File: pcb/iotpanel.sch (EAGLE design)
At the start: 33 parts, among them IC1 IC_CPLD_XC2C32A, IC4 REG1117, IC5 REG1117

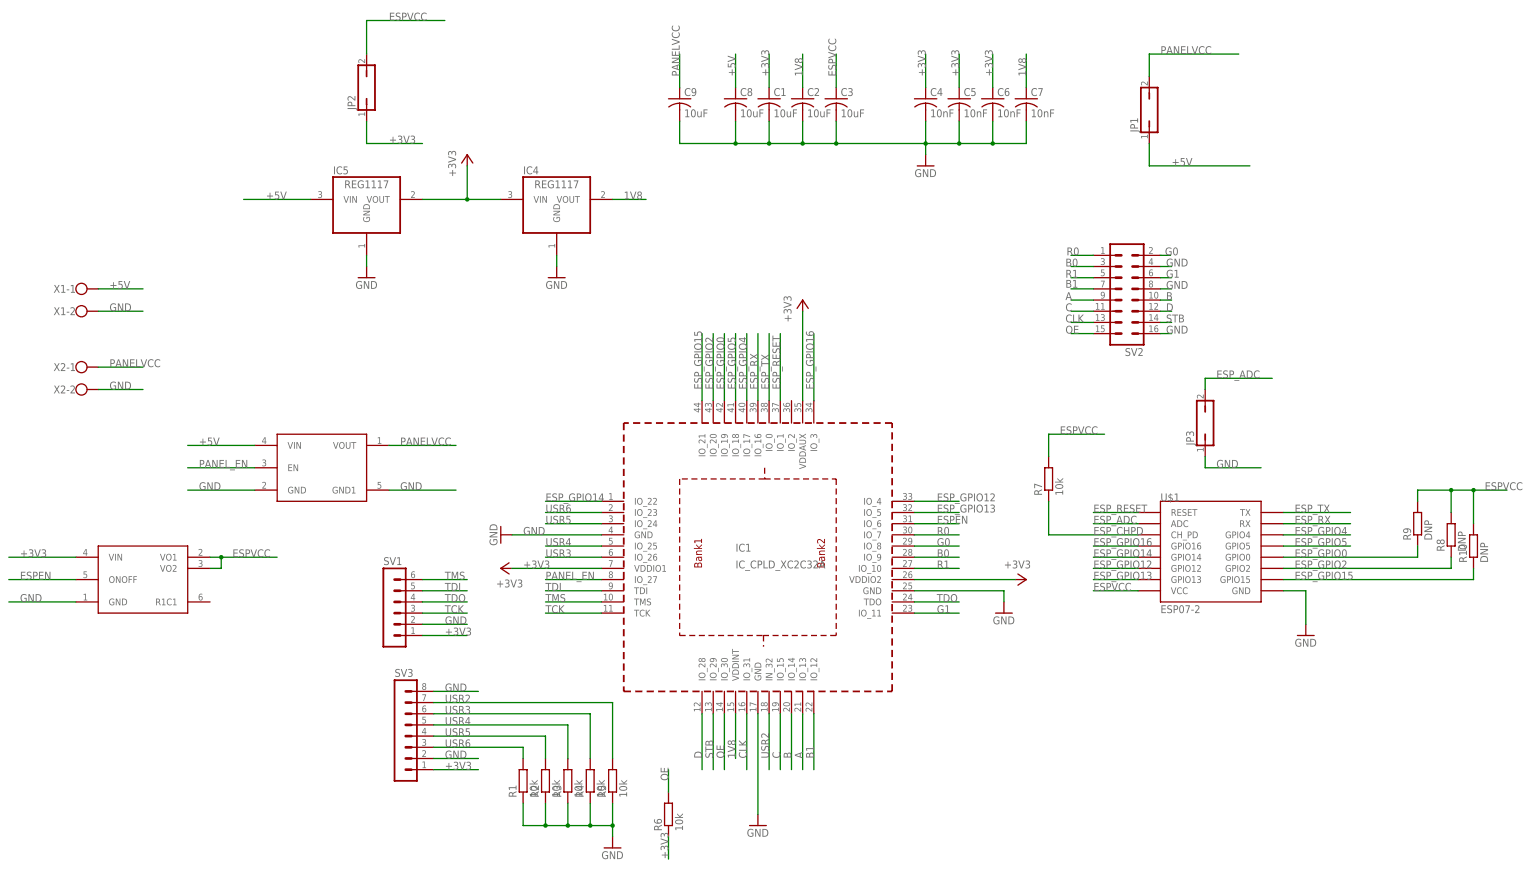
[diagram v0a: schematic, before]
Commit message: Add v1.1 board
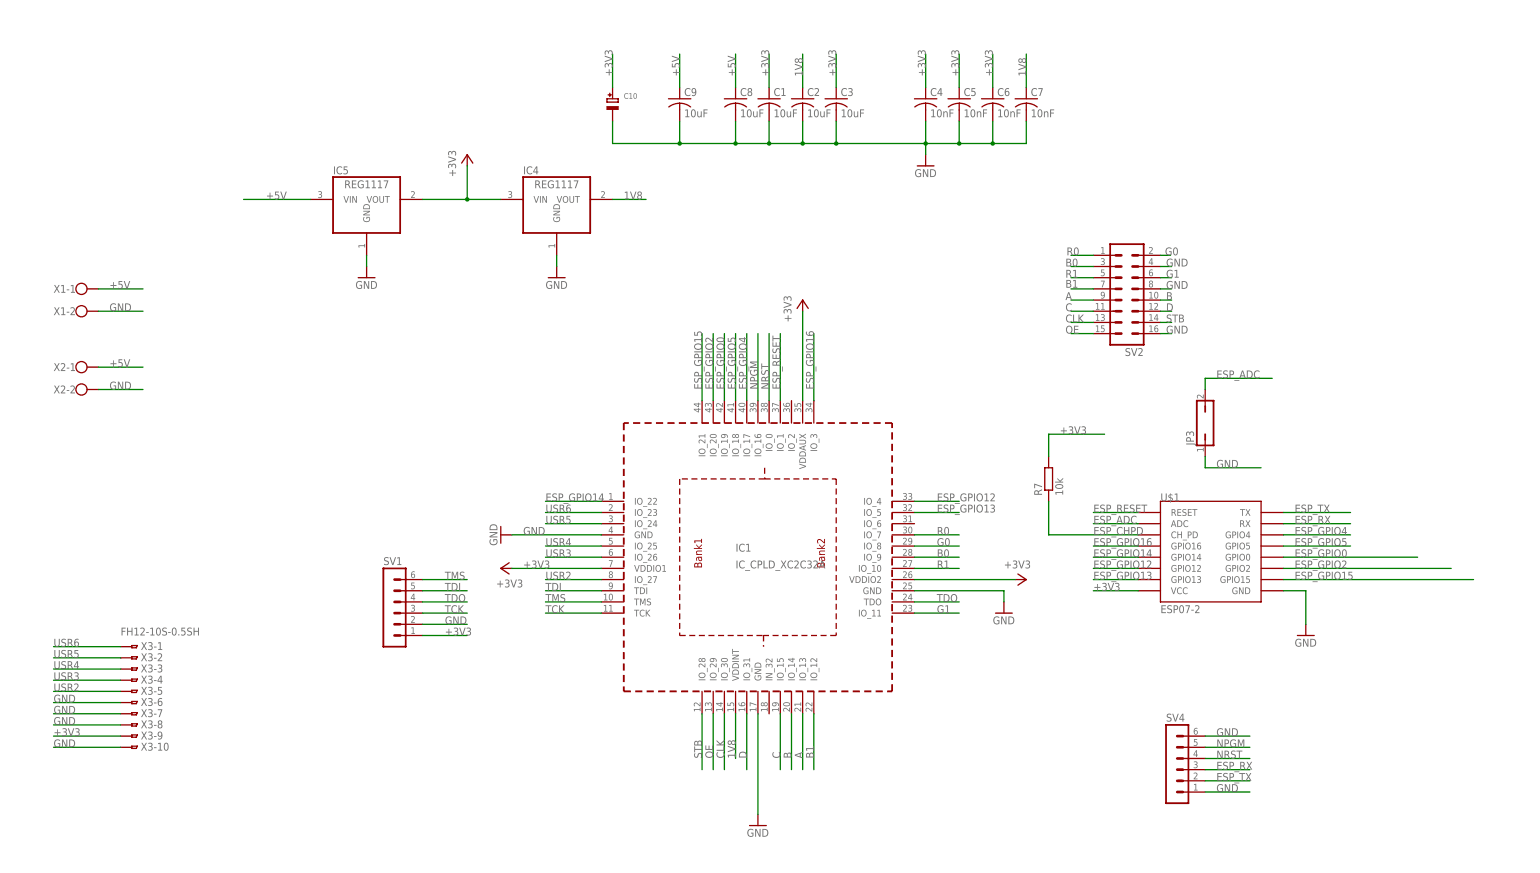
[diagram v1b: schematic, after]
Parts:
- removed JP1, JP2: (no value), jumper:JP1Q
- removed R1, R2, R3, R4, R5, R6: 10k, rcl:R-EU_R0805
- removed R10, R8, R9: DNP, rcl:R-EU_R0805
- removed SV3: (no value), con-lstb:MA08-1
- removed U$2: MIC9406XBC6, alvie:MIC9406XBC6
- removed U$3: SI1867DL, alvie:SI1867DL
- added C10: (no value), microbuilder:CAP_TANTALUMA/3216_WAVE
- added SV4: (no value), con-lstb:MA06-1
- added X3: FH12-10S-0.5SH, con-hirose:FH12-10S-0.5SH
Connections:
- removed net ESPEN: IC1.IO_6, U$3.ONOFF
- removed net ESPVCC: C3.1, JP2.2, R10.2, R7.2, R8.2, R9.2, U$1.VCC, U$3.VO1, U$3.VO2
- removed net PANELVCC: C9.1, JP1.2, U$2.VOUT, X2-1.KL
- removed net PANEL_EN: IC1.IO_27, U$2.EN
- new net NPGM: IC1.IO_16, SV4.5
- new net NRST: IC1.IO_0, SV4.4
- net +3V3: now also C10.+, C3.1, R7.2, U$1.VCC, X3-9.1; no longer JP2.1, R6.1, SV3.1, U$3.VIN
- net +5V: now also C9.1, X2-1.KL; no longer JP1.1, U$2.VIN
- net CLK: now also IC1.IO_30; no longer IC1.IO_31
- net D: now also IC1.IO_31; no longer IC1.IO_28
- net ESP_GPIO0: no longer R9.1
- net ESP_GPIO15: no longer R10.1
- net ESP_GPIO2: no longer R8.1
- net ESP_RX: now also SV4.3; no longer IC1.IO_16
- net ESP_TX: now also SV4.2; no longer IC1.IO_0
- net GND: now also C10.-, SV4.1, SV4.6, X3-10.1, X3-6.1, X3-7.1, X3-8.1; no longer R1.1, R2.1, R3.1, R4.1, R5.1, SV3.2, SV3.8, U$2.GND, U$2.GND1, U$3.GND
- net OE: now also IC1.IO_29; no longer IC1.IO_30, R6.2
- net STB: now also IC1.IO_28; no longer IC1.IO_29
- net USR2: now also IC1.IO_27, X3-5.1; no longer IC1.IN_32, R5.2, SV3.7
- net USR3: now also X3-4.1; no longer R4.2, SV3.6
- net USR4: now also X3-3.1; no longer R3.2, SV3.5
- net USR5: now also X3-2.1; no longer R2.2, SV3.4
- net USR6: now also X3-1.1; no longer R1.2, SV3.3
